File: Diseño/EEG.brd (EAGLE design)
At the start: 49.8 x 80 mm, 41 parts, among them IC1 REF2033AIDDCT, IC2 MCP73831T-2ACI_OT, IC3 LP38692MP-3.3_NOPB, J1 USB3500-30-A-KIT, J2 SJ3-35083A-TR, J3 1769

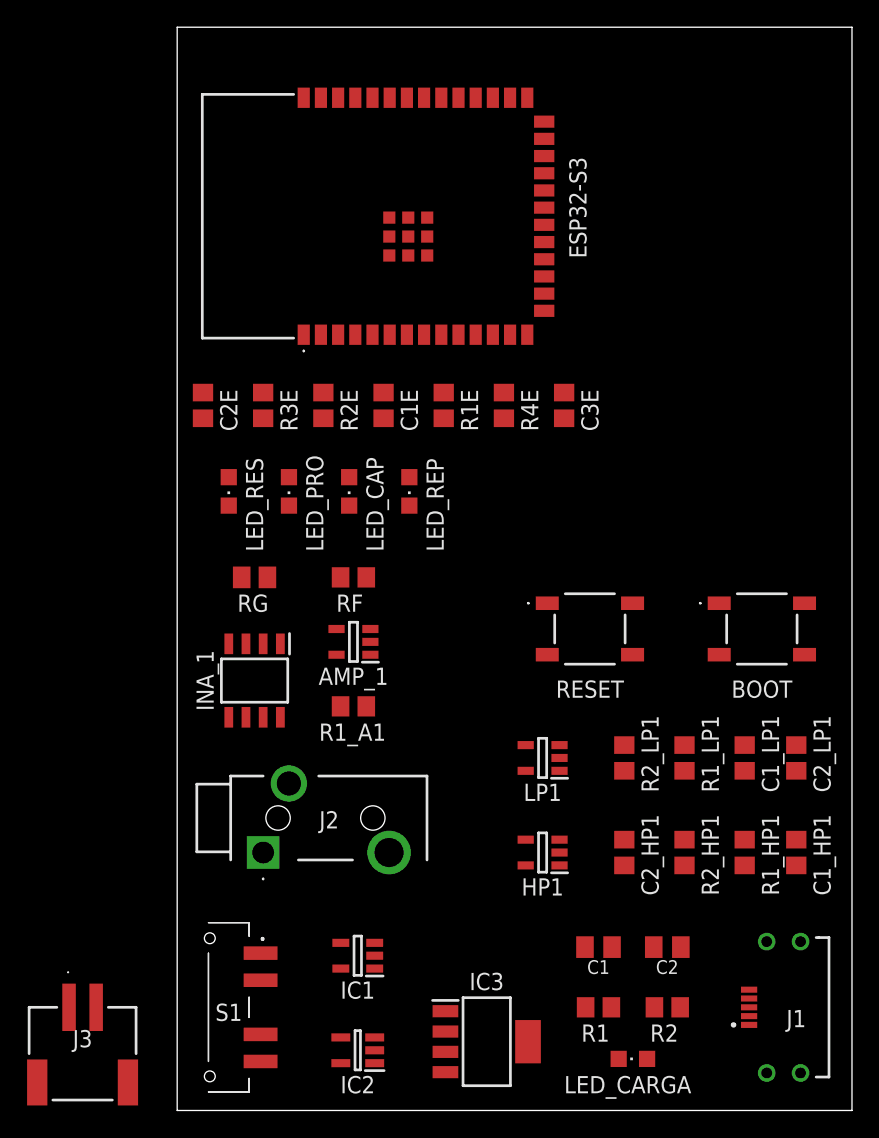
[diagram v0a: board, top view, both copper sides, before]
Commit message: enrutamiento y cambios en la conexion de bateria, Falta GND
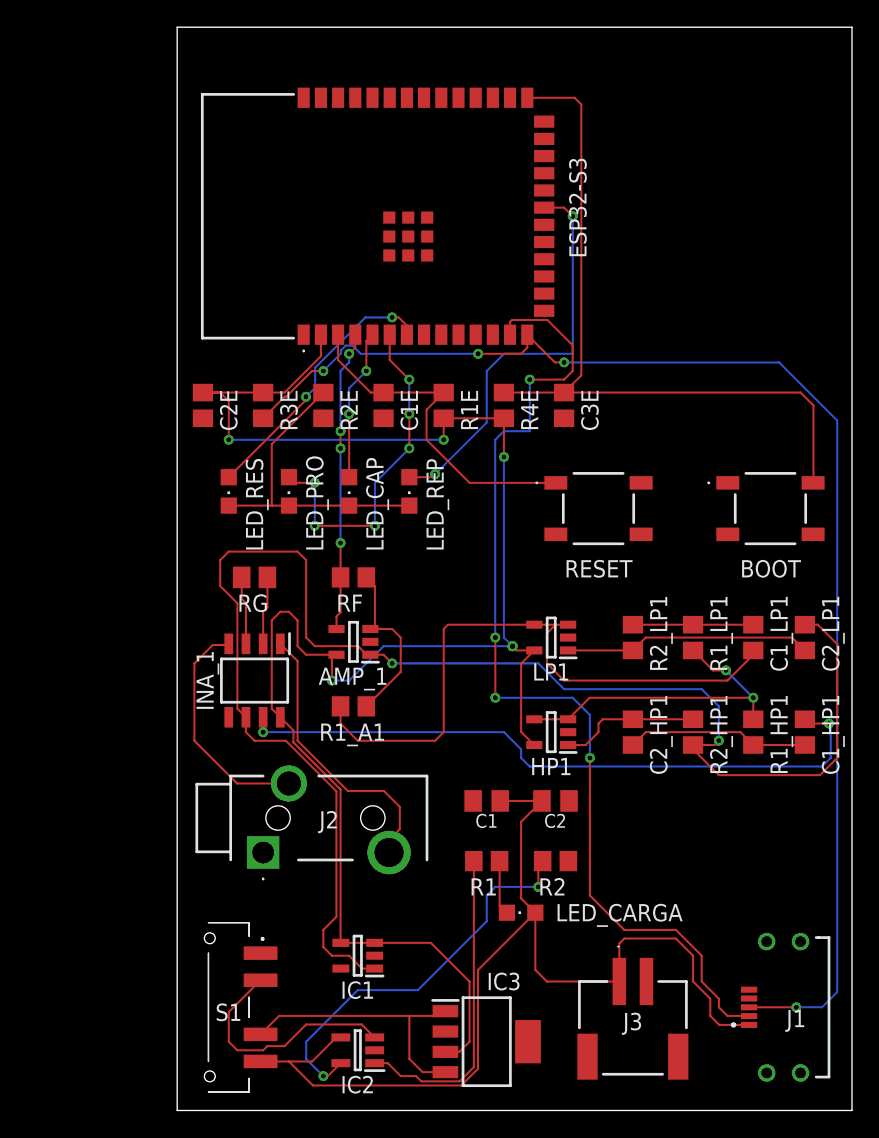
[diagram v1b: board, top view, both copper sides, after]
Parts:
- moved J3 40.7 mm to (33.7, 9.53)
- moved LED_CARGA 13.6 mm to (25.4, 14.6)
- moved C1 13.6 mm to (22.9, 22.9)
- moved C2 13.6 mm to (27.9, 22.9)
- moved R1 13.6 mm to (22.9, 18.4)
- moved R2 13.6 mm to (27.9, 18.4)
- moved BOOT 8.91 mm to (43.8, 44.5)
- moved C1_HP1 8.91 mm to (46.4, 27.9)
- moved C2_HP1 8.91 mm to (33.7, 27.9)
- moved HP1 8.91 mm to (27.6, 27.9)
- moved R1_HP1 8.91 mm to (42.5, 27.9)
- moved R2_HP1 8.91 mm to (38.1, 27.9)
- moved RESET 8.91 mm to (31.1, 44.5)
- moved C1_LP1 8.91 mm to (42.5, 34.9)
- moved C2_LP1 8.91 mm to (46.4, 34.9)
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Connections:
- net +5V: now also J3.1; no longer J3.3
- net GND: now also J1.4, J3.2; no longer J3.4
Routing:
- net +3V3: track 0.00 -> 131.9 mm, vias 0 -> 6
- net VSS: track 0.00 -> 111.7 mm, vias 0 -> 2
- net USB_3: track 0.00 -> 98.2 mm, vias 0 -> 4
- net +5V: track 0.00 -> 75.4 mm
- net USB_2: track 0.00 -> 75.2 mm, vias 0 -> 4
- net N$13: track 0.00 -> 55.0 mm
- net O1: track 0.00 -> 49.3 mm, vias 0 -> 2
- net O3: track 0.00 -> 46.6 mm
- net LED_REP: track 0.00 -> 30.6 mm, vias 0 -> 2
- net N$2: track 0.00 -> 29.8 mm, vias 0 -> 2
- net N$19: track 0.00 -> 25.5 mm
- net N$16: track 0.00 -> 25.5 mm, vias 0 -> 6
- net O2: track 0.00 -> 24.3 mm, vias 0 -> 2
- net N$10: track 0.00 -> 23.6 mm
- net N$15: track 0.00 -> 23.3 mm
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
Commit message: Corrección Esp-32
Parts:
- removed R3E: 1.5K, rcl:R0805
- added R3, R4: 22, rcl:R0805
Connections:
- new net N$14: ESP32-S3.14, R4.2
- new net N$18: ESP32-S3.13, R3.2
- net +3V3: no longer R3E.1
- net USB_2: now also R3.1; no longer ESP32-S3.13
- net USB_3: now also R4.1; no longer ESP32-S3.14, R3E.2
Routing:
- net USB_3: track 98.2 -> 71.8 mm, vias 4 -> 2
- net +3V3: track 131.9 -> 125.9 mm
- net USB_2: track 75.2 -> 74.2 mm
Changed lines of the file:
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@@
 <drawing>
 <settings>
-<setting alwaysvectorfont="yes"/>
+<setting alwaysvectorfont="no"/>
 <setting verticaltext="up"/>
 </settings>
@@
 <attribute name="VALUE" x="31.115" y="50.8" size="1.27" layer="27" rot="R90"/>
 </element>
-<element name="R3E" library="rcl" library_urn="urn:adsk.eagle:library:334" package="R0805" package3d_urn="urn:adsk.eagle:package:23553/2" value="1.5K" x="6.35" y="52.07" smashed="yes" rot="R270">
-<attribute name="NAME" x="8.89" y="50.165" size="1.27" layer="25" rot="R90"/>
-<attribute name="POPULARITY" value="86" x="6.35" y="52.07" size="1.778" layer="27" rot="R270" display="off"/>
-<attribute name="SPICEPREFIX" value="R" x="6.35" y="52.07" size="1.778" layer="27" rot="R270" display="off"/>
-<attribute name="VALUE" x="3.81" y="52.705" size="1.27" layer="27" rot="R270"/>
-</element>
 <element name="LED_REP" library="led" library_urn="urn:adsk.eagle:library:259" package="CHIPLED_0805" package3d_urn="urn:adsk.eagle:package:15821/2" value="" x="17.145" y="45.72" smashed="yes" rot="R180">
 <attribute name="NAME" x="19.685" y="41.275" size="1.27" layer="25" rot="R90"/>
@@
 <attribute name="NAME" x="33.655" y="6.569" size="1.27" layer="25" align="center"/>
 <attribute name="VALUE" x="33.655" y="7.204" size="1.27" layer="27" align="center"/>
+</element>
+<element name="R3" library="rcl" library_urn="urn:adsk.eagle:library:334" package="R0805" package3d_urn="urn:adsk.eagle:package:23553/2" value="22" x="22.225" y="39.37" smashed="yes" rot="R90">
+<attribute name="NAME" x="20.955" y="38.735" size="1.27" layer="25" rot="R90"/>
+<attribute name="POPULARITY" value="86" x="22.225" y="39.37" size="1.778" layer="27" rot="R90" display="off"/>
+<attribute name="SPICEPREFIX" value="R" x="22.225" y="39.37" size="1.778" layer="27" rot="R90" display="off"/>
+<attribute name="VALUE" x="24.765" y="38.735" size="1.27" layer="27" rot="R90"/>
+</element>
+<element name="R4" library="rcl" library_urn="urn:adsk.eagle:library:334" package="R0805" package3d_urn="urn:adsk.eagle:package:23553/2" value="22" x="36.195" y="59.69" smashed="yes" rot="R90">
+<attribute name="NAME" x="34.925" y="59.055" size="1.27" layer="25" rot="R90"/>
+<attribute name="POPULARITY" value="86" x="36.195" y="59.69" size="1.778" layer="27" rot="R90" display="off"/>
+<attribute name="SPICEPREFIX" value="R" x="36.195" y="59.69" size="1.778" layer="27" rot="R90" display="off"/>
+<attribute name="VALUE" x="38.735" y="59.055" size="1.27" layer="27" rot="R90"/>
 </element>
 </elements>
@@
 <contactref element="HP1" pad="5"/>
 <contactref element="LP1" pad="5"/>
-<contactref element="R3E" pad="1"/>
 <contactref element="IC3" pad="3"/>
-<wire x1="7.935" y1="53.02" x2="6.35" y2="53.02" width="0.1524" layer="1"/>
 <wire x1="10.615" y1="55.7" x2="7.935" y2="53.02" width="0.1524" layer="1"/>
 <wire x1="19.685" y1="51.12" x2="24.13" y2="51.12" width="0.1524" layer="1"/>
@@
 <wire x1="24.13" y1="48.26" x2="24.13" y2="51.12" width="0.1524" layer="1"/>
 <wire x1="10.615" y1="57.29" x2="10.615" y2="55.7" width="0.1524" layer="1"/>
-<wire x1="1.905" y1="53.02" x2="6.35" y2="53.02" width="0.1524" layer="1"/>
 <via x="3.81" y="49.53" extent="1-16" drill="0.35"/>
 <wire x1="3.81" y1="49.53" x2="19.685" y2="49.53" width="0.1524" layer="16"/>
@@
 <wire x1="3.81" y1="52.385" x2="3.81" y2="49.53" width="0.1524" layer="1"/>
 <wire x1="19.685" y1="51.12" x2="19.685" y2="49.53" width="0.1524" layer="1"/>
+<wire x1="3.81" y1="49.53" x2="7.935" y2="53.02" width="0" layer="19" extent="1-1"/>
 </signal>
 <signal name="GND">
@@
 <signal name="USB_2">
 <contactref element="J1" pad="2"/>
-<contactref element="ESP32-S3" pad="13"/>
 <wire x1="42.2375" y1="6.97" x2="42.2225" y2="6.985" width="0.1524" layer="1"/>
 <wire x1="42.2225" y1="6.985" x2="40.64" y2="6.985" width="0.1524" layer="1"/>
@@
 <wire x1="30.48" y1="15.875" x2="30.48" y2="26.035" width="0.1524" layer="1"/>
 <wire x1="23.495" y1="34.925" x2="23.495" y2="49.53" width="0.1524" layer="16"/>
-<wire x1="24.585" y1="58.24" x2="24.585" y2="57.29" width="0.1524" layer="1"/>
 <wire x1="29.21" y1="56.515" x2="29.21" y2="54.61" width="0.1524" layer="1"/>
 <wire x1="29.21" y1="54.61" x2="28.575" y2="53.975" width="0.1524" layer="1"/>
@@
 <wire x1="24.7214" y1="58.3764" x2="24.585" y2="58.24" width="0.1524" layer="1"/>
 <wire x1="27.3486" y1="58.3764" x2="24.7214" y2="58.3764" width="0.1524" layer="1"/>
+<contactref element="R3" pad="1"/>
+<wire x1="23.495" y1="34.925" x2="22.225" y2="38.42" width="0" layer="19" extent="1-1"/>
 </signal>
 <signal name="USB_3">
 <contactref element="J1" pad="3"/>
-<contactref element="ESP32-S3" pad="14"/>
-<contactref element="R3E" pad="2"/>
-<via x="10.795" y="54.61" extent="1-16" drill="0.35"/>
-<wire x1="6.35" y1="51.12" x2="7.9452" y2="52.7152" width="0.1524" layer="1"/>
-<wire x1="7.9452" y1="52.7152" x2="8.06125625" y2="52.7152" width="0.1524" layer="1"/>
-<wire x1="8.06125625" y1="52.7152" x2="9.95605625" y2="54.61" width="0.1524" layer="1"/>
-<wire x1="9.95605625" y1="54.61" x2="10.795" y2="54.61" width="0.1524" layer="1"/>
-<via x="22.225" y="55.88" extent="1-16" drill="0.35"/>
-<wire x1="12.0932" y1="56.13135" x2="12.44865" y2="56.4868" width="0.1524" layer="16"/>
-<wire x1="12.44865" y1="56.4868" x2="12.95135" y2="56.4868" width="0.1524" layer="16"/>
-<wire x1="12.0932" y1="55.9082" x2="12.0932" y2="56.13135" width="0.1524" layer="16"/>
-<wire x1="13.55815" y1="55.88" x2="22.225" y2="55.88" width="0.1524" layer="16"/>
-<wire x1="10.795" y1="54.61" x2="12.0932" y2="55.9082" width="0.1524" layer="16"/>
-<wire x1="12.95135" y1="56.4868" x2="13.55815" y2="55.88" width="0.1524" layer="16"/>
-<wire x1="26.035" y1="57.11" x2="25.855" y2="57.29" width="0.1524" layer="1"/>
-<wire x1="25.855" y1="57.29" x2="25.855" y2="56.335" width="0.1524" layer="1"/>
-<wire x1="25.855" y1="56.335" x2="25.4" y2="55.88" width="0.1524" layer="1"/>
-<wire x1="25.4" y1="55.88" x2="22.225" y2="55.88" width="0.1524" layer="1"/>
-<wire x1="25.855" y1="57.29" x2="27.9" y2="55.245" width="0.1524" layer="1"/>
 <wire x1="27.9" y1="55.245" x2="28.575" y2="55.245" width="0.1524" layer="1"/>
 <via x="28.575" y="55.245" extent="1-16" drill="0.35"/>
@@
 <wire x1="44.45" y1="55.245" x2="48.7428" y2="50.9522" width="0.1524" layer="16"/>
 <wire x1="48.7428" y1="50.9522" x2="48.7428" y2="8.7378" width="0.1524" layer="16"/>
+<contactref element="R4" pad="1"/>
+<wire x1="27.9" y1="55.245" x2="36.195" y2="58.74" width="0" layer="19" extent="1-1"/>
 </signal>
 <signal name="RX">
@@
 <wire x1="6.985" y1="49.21" x2="6.985" y2="44.67" width="0.1524" layer="1"/>
 </signal>
+<signal name="N$14">
+<contactref element="ESP32-S3" pad="14"/>
+<contactref element="R4" pad="2"/>
+<wire x1="25.855" y1="57.29" x2="36.195" y2="60.64" width="0" layer="19" extent="1-1"/>
+</signal>
+<signal name="N$18">
+<contactref element="ESP32-S3" pad="13"/>
+<contactref element="R3" pad="2"/>
+<wire x1="22.225" y1="40.32" x2="24.585" y2="57.29" width="0" layer="19" extent="1-1"/>
+</signal>
 </signals>

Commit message: añadido paths de resistencias de programación
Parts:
- moved R4 7.85 mm to (34.3, 52.1)
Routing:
- net USB_2: track 74.2 -> 50.8 mm
- net N$18: track 0.00 -> 19.3 mm, vias 0 -> 4
- net N$14: track 0.00 -> 10.2 mm, vias 0 -> 2
- net USB_3: track 71.8 -> 64.0 mm
- net +3V3: track 125.9 -> 130.1 mm
- net N$13: track 55.0 -> 51.6 mm
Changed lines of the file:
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@@
 <attribute name="VALUE" x="24.765" y="38.735" size="1.27" layer="27" rot="R90"/>
 </element>
-<element name="R4" library="rcl" library_urn="urn:adsk.eagle:library:334" package="R0805" package3d_urn="urn:adsk.eagle:package:23553/2" value="22" x="36.195" y="59.69" smashed="yes" rot="R90">
-<attribute name="NAME" x="34.925" y="59.055" size="1.27" layer="25" rot="R90"/>
-<attribute name="POPULARITY" value="86" x="36.195" y="59.69" size="1.778" layer="27" rot="R90" display="off"/>
-<attribute name="SPICEPREFIX" value="R" x="36.195" y="59.69" size="1.778" layer="27" rot="R90" display="off"/>
-<attribute name="VALUE" x="38.735" y="59.055" size="1.27" layer="27" rot="R90"/>
+<element name="R4" library="rcl" library_urn="urn:adsk.eagle:library:334" package="R0805" package3d_urn="urn:adsk.eagle:package:23553/2" value="22" x="34.29" y="52.07" smashed="yes" rot="R90">
+<attribute name="NAME" x="33.02" y="51.435" size="1.27" layer="25" rot="R90"/>
+<attribute name="POPULARITY" value="86" x="34.29" y="52.07" size="1.778" layer="27" rot="R90" display="off"/>
+<attribute name="SPICEPREFIX" value="R" x="34.29" y="52.07" size="1.778" layer="27" rot="R90" display="off"/>
+<attribute name="VALUE" x="36.83" y="51.435" size="1.27" layer="27" rot="R90"/>
 </element>
 </elements>
@@
 <wire x1="10.615" y1="57.29" x2="10.615" y2="55.7" width="0.1524" layer="1"/>
 <via x="3.81" y="49.53" extent="1-16" drill="0.35"/>
-<wire x1="3.81" y1="49.53" x2="19.685" y2="49.53" width="0.1524" layer="16"/>
+<wire x1="3.81" y1="49.53" x2="8.89" y2="54.61" width="0.1524" layer="16"/>
+<wire x1="14.605" y1="54.61" x2="8.89" y2="54.61" width="0.1524" layer="16"/>
+<wire x1="14.605" y1="54.61" x2="19.685" y2="49.53" width="0.1524" layer="16"/>
 <via x="19.685" y="49.53" extent="1-16" drill="0.35"/>
 <wire x1="1.905" y1="53.02" x2="3.175" y2="53.02" width="0.1524" layer="1"/>
@@
 <wire x1="3.81" y1="52.385" x2="3.81" y2="49.53" width="0.1524" layer="1"/>
 <wire x1="19.685" y1="51.12" x2="19.685" y2="49.53" width="0.1524" layer="1"/>
-<wire x1="3.81" y1="49.53" x2="7.935" y2="53.02" width="0" layer="19" extent="1-1"/>
+<wire x1="14.605" y1="54.61" x2="7.935" y2="53.02" width="0" layer="19" extent="1-1"/>
 </signal>
 <signal name="GND">
@@
 <contactref element="R4E" pad="1"/>
 <contactref element="BOOT" pad="2"/>
-<wire x1="46.04" y1="53.02" x2="46.99" y2="52.07" width="0.1524" layer="1"/>
-<wire x1="46.99" y1="52.07" x2="46.99" y2="46.375" width="0.1524" layer="1"/>
-<wire x1="46.99" y1="46.375" x2="46.965" y2="46.35" width="0.1524" layer="1"/>
+<wire x1="46.99" y1="46.375" x2="46.98" y2="46.365" width="0.1524" layer="1"/>
 <wire x1="28.575" y1="53.02" x2="24.13" y2="53.02" width="0.1524" layer="1"/>
-<wire x1="28.575" y1="53.02" x2="46.04" y2="53.02" width="0.1524" layer="1"/>
 <wire x1="28.575" y1="53.02" x2="29.845" y2="54.29" width="0.1524" layer="1"/>
 <wire x1="29.845" y1="74.295" x2="29.35" y2="74.79" width="0.1524" layer="1"/>
 <wire x1="29.35" y1="74.79" x2="25.855" y2="74.79" width="0.1524" layer="1"/>
 <wire x1="29.845" y1="54.29" x2="29.845" y2="74.295" width="0.1524" layer="1"/>
+<wire x1="28.575" y1="53.02" x2="32.7" y2="48.895" width="0.1524" layer="1"/>
+<wire x1="44.45" y1="48.895" x2="46.98" y2="46.365" width="0.1524" layer="1"/>
+<wire x1="32.7" y1="48.895" x2="44.45" y2="48.895" width="0.1524" layer="1"/>
+<wire x1="46.965" y1="46.35" x2="46.98" y2="46.365" width="0.1524" layer="1"/>
 </signal>
 <signal name="USB_2">
@@
 <wire x1="23.495" y1="30.48" x2="23.495" y2="34.925" width="0.1524" layer="1"/>
 <via x="23.495" y="34.925" extent="1-16" drill="0.35"/>
-<wire x1="23.495" y1="49.53" x2="24.13" y2="50.165" width="0.1524" layer="16"/>
-<wire x1="24.13" y1="50.165" x2="26.035" y2="50.165" width="0.1524" layer="16"/>
-<wire x1="26.035" y1="50.165" x2="26.035" y2="53.975" width="0.1524" layer="16"/>
 <wire x1="38.735" y1="11.43" x2="36.83" y2="13.335" width="0.1524" layer="1"/>
 <wire x1="30.48" y1="15.875" x2="30.48" y2="26.035" width="0.1524" layer="1"/>
-<wire x1="23.495" y1="34.925" x2="23.495" y2="49.53" width="0.1524" layer="16"/>
-<wire x1="29.21" y1="56.515" x2="29.21" y2="54.61" width="0.1524" layer="1"/>
-<wire x1="29.21" y1="54.61" x2="28.575" y2="53.975" width="0.1524" layer="1"/>
-<wire x1="29.21" y1="56.515" x2="27.3486" y2="58.3764" width="0.1524" layer="1"/>
-<via x="26.035" y="53.975" extent="1-16" drill="0.35"/>
-<wire x1="28.575" y1="53.975" x2="26.035" y2="53.975" width="0.1524" layer="1"/>
-<wire x1="24.7214" y1="58.3764" x2="24.585" y2="58.24" width="0.1524" layer="1"/>
-<wire x1="27.3486" y1="58.3764" x2="24.7214" y2="58.3764" width="0.1524" layer="1"/>
 <contactref element="R3" pad="1"/>
-<wire x1="23.495" y1="34.925" x2="22.225" y2="38.42" width="0" layer="19" extent="1-1"/>
+<wire x1="22.225" y1="38.42" x2="20.005" y2="38.42" width="0.1524" layer="1"/>
+<wire x1="20.005" y1="38.42" x2="19.685" y2="38.1" width="0.1524" layer="1"/>
+<via x="19.685" y="36.83" extent="1-16" drill="0.35"/>
+<wire x1="19.685" y1="36.83" x2="21.59" y2="34.925" width="0.1524" layer="16"/>
+<wire x1="21.59" y1="34.925" x2="23.495" y2="34.925" width="0.1524" layer="16"/>
+<wire x1="19.685" y1="38.1" x2="19.685" y2="36.83" width="0.1524" layer="1"/>
 </signal>
 <signal name="USB_3">
 <contactref element="J1" pad="3"/>
-<wire x1="27.9" y1="55.245" x2="28.575" y2="55.245" width="0.1524" layer="1"/>
-<via x="28.575" y="55.245" extent="1-16" drill="0.35"/>
-<wire x1="28.575" y1="55.245" x2="44.45" y2="55.245" width="0.1524" layer="16"/>
 <wire x1="48.7428" y1="8.7378" x2="47.625" y2="7.62" width="0.1524" layer="16"/>
 <wire x1="47.625" y1="7.62" x2="45.72" y2="7.62" width="0.1524" layer="16"/>
 <via x="45.72" y="7.62" extent="1-16" drill="0.35"/>
 <wire x1="45.72" y1="7.62" x2="42.2375" y2="7.62" width="0.1524" layer="1"/>
-<wire x1="44.45" y1="55.245" x2="48.7428" y2="50.9522" width="0.1524" layer="16"/>
-<wire x1="48.7428" y1="50.9522" x2="48.7428" y2="8.7378" width="0.1524" layer="16"/>
+<wire x1="48.7428" y1="8.7378" x2="48.7428" y2="50.9522" width="0.1524" layer="16"/>
 <contactref element="R4" pad="1"/>
-<wire x1="27.9" y1="55.245" x2="36.195" y2="58.74" width="0" layer="19" extent="1-1"/>
+<wire x1="48.7428" y1="50.9522" x2="48.26" y2="51.435" width="0.1524" layer="16"/>
+<via x="40.005" y="51.435" extent="1-16" drill="0.35"/>
+<wire x1="40.005" y1="51.435" x2="39.69" y2="51.12" width="0.1524" layer="1"/>
+<wire x1="39.69" y1="51.12" x2="34.29" y2="51.12" width="0.1524" layer="1"/>
+<wire x1="48.26" y1="51.435" x2="40.005" y2="51.435" width="0.1524" layer="16"/>
 </signal>
 <signal name="RX">
@@
 <contactref element="ESP32-S3" pad="14"/>
 <contactref element="R4" pad="2"/>
-<wire x1="25.855" y1="57.29" x2="36.195" y2="60.64" width="0" layer="19" extent="1-1"/>
+<wire x1="25.855" y1="57.29" x2="28.535" y2="54.61" width="0.1524" layer="1"/>
+<wire x1="28.535" y1="54.61" x2="28.575" y2="54.61" width="0.1524" layer="1"/>
+<via x="28.575" y="54.61" extent="1-16" drill="0.35"/>
+<wire x1="28.575" y1="54.61" x2="31.115" y2="54.61" width="0.1524" layer="16"/>
+<via x="31.115" y="54.61" extent="1-16" drill="0.35"/>
+<wire x1="34.29" y1="53.02" x2="32.7" y2="54.61" width="0.1524" layer="1"/>
+<wire x1="32.7" y1="54.61" x2="31.115" y2="54.61" width="0.1524" layer="1"/>
 </signal>
 <signal name="N$18">
 <contactref element="ESP32-S3" pad="13"/>
 <contactref element="R3" pad="2"/>
-<wire x1="22.225" y1="40.32" x2="24.585" y2="57.29" width="0" layer="19" extent="1-1"/>
+<wire x1="24.585" y1="57.29" x2="23.9936" y2="56.6986" width="0.1524" layer="1"/>
+<wire x1="23.9936" y1="56.6986" x2="23.9936" y2="56.4453125" width="0.1524" layer="1"/>
+<wire x1="23.9936" y1="56.4453125" x2="22.225" y2="54.6767125" width="0.1524" layer="1"/>
+<via x="22.225" y="52.07" extent="1-16" drill="0.35"/>
+<wire x1="22.225" y1="52.07" x2="22.225" y2="50.8" width="0.1524" layer="16"/>
+<wire x1="22.225" y1="50.8" x2="20.955" y2="49.53" width="0.1524" layer="16"/>
+<wire x1="20.955" y1="49.53" x2="20.843425" y2="49.641575" width="0.1524" layer="16"/>
+<via x="20.843425" y="49.641575" extent="1-16" drill="0.35"/>
+<wire x1="20.843425" y1="49.641575" x2="21.59" y2="48.895" width="0.1524" layer="1"/>
+<via x="21.59" y="47.625" extent="1-16" drill="0.35"/>
+<wire x1="21.59" y1="47.625" x2="21.59" y2="45.085" width="0.1524" layer="16"/>
+<via x="21.59" y="45.085" extent="1-16" drill="0.35"/>
+<wire x1="21.59" y1="45.085" x2="21.59" y2="40.955" width="0.1524" layer="1"/>
+<wire x1="21.59" y1="40.955" x2="22.225" y2="40.32" width="0.1524" layer="1"/>
+<wire x1="22.225" y1="54.6767125" x2="22.225" y2="52.07" width="0.1524" layer="1"/>
+<wire x1="21.59" y1="48.895" x2="21.59" y2="47.625" width="0.1524" layer="1"/>
 </signal>
 </signals>
